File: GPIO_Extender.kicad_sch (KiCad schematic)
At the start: 22 parts, among them IC1 PCA9575PW2,118

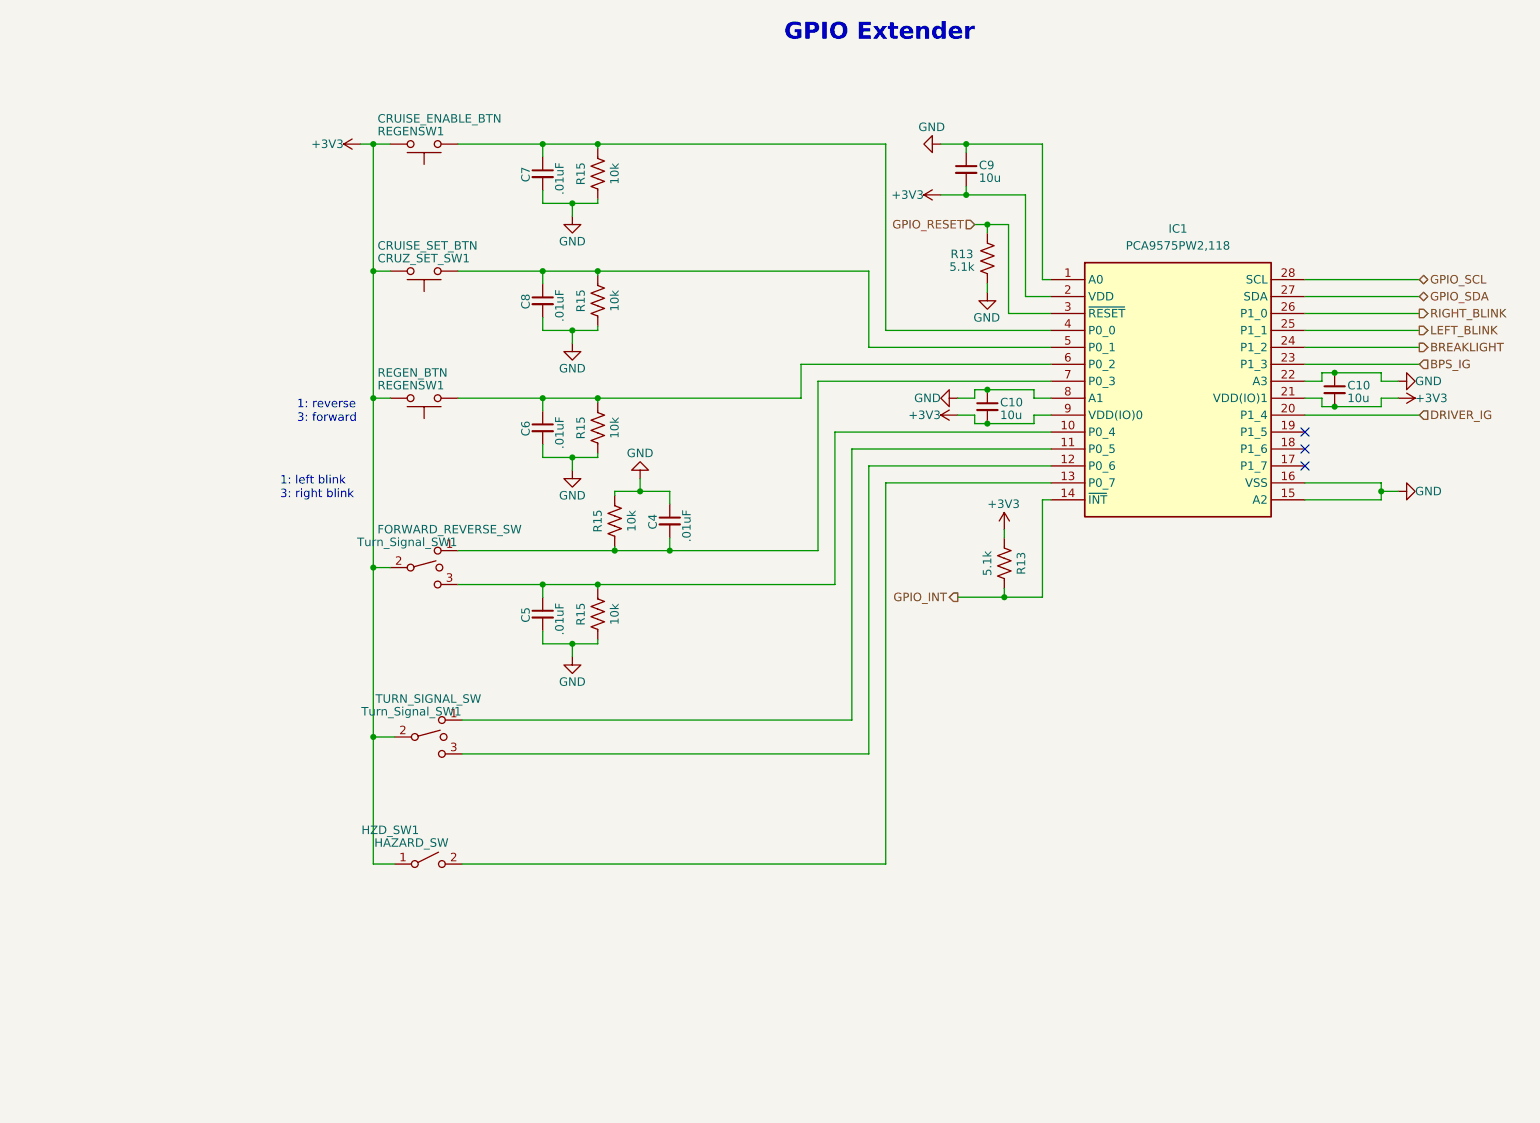
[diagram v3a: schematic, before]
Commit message: added notes section to bottom of sheets
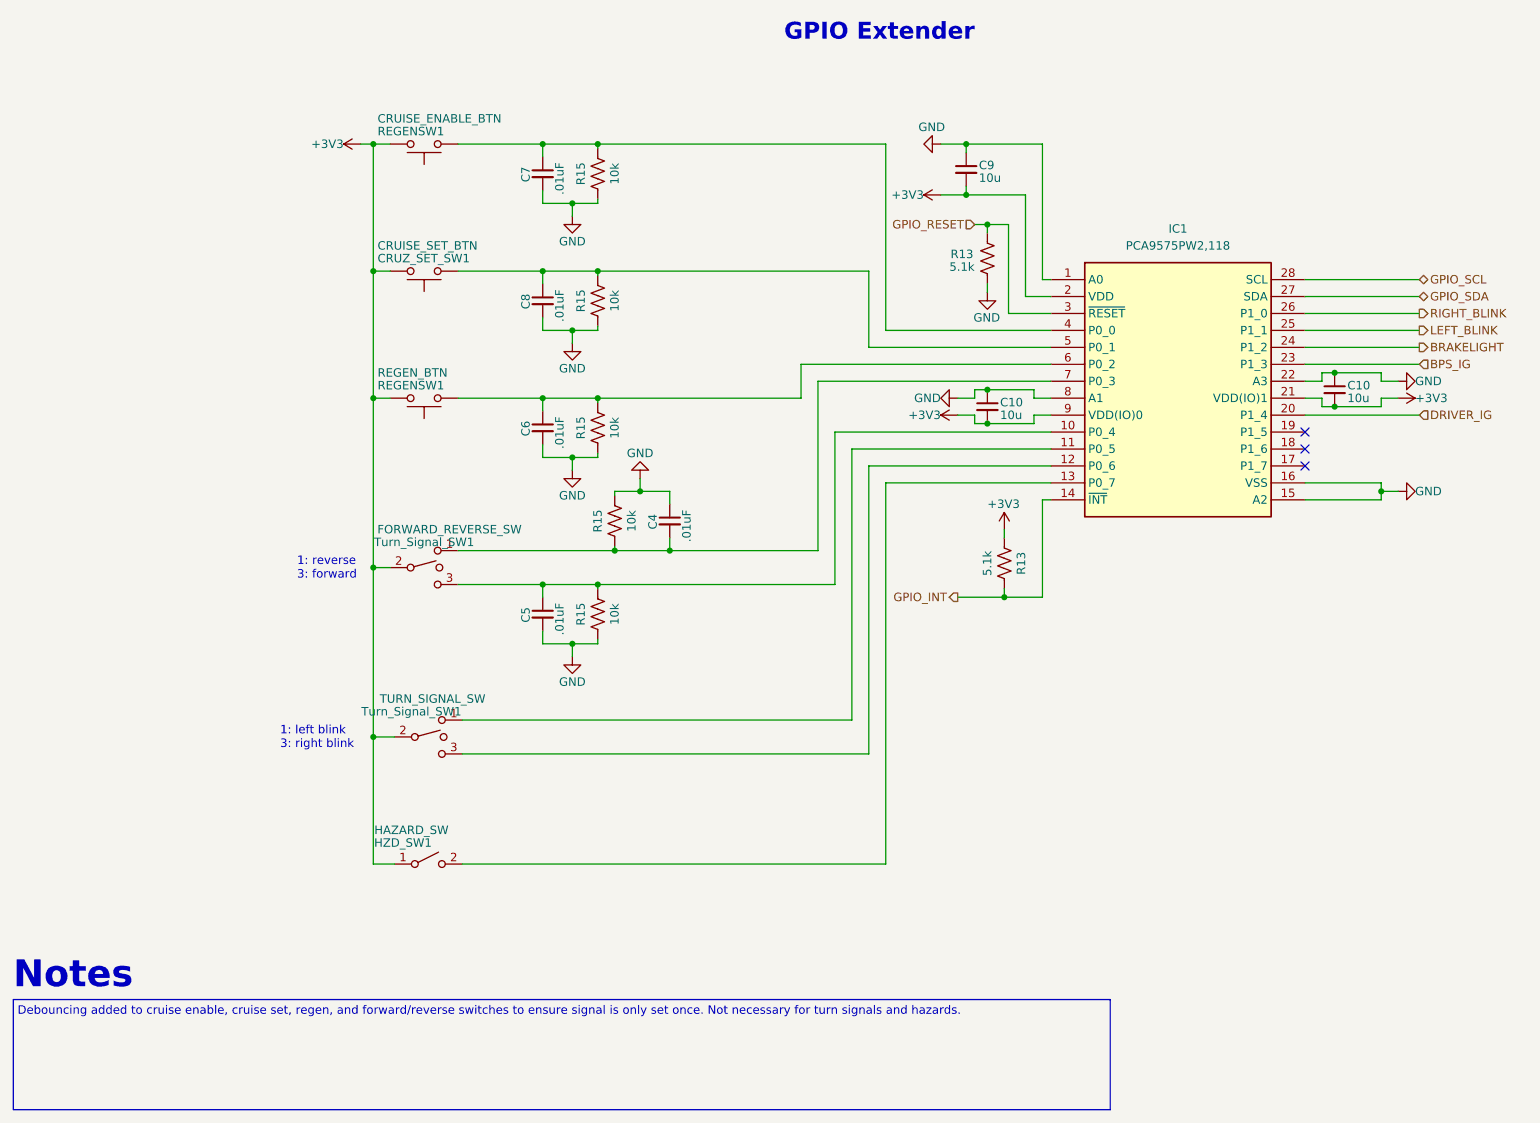
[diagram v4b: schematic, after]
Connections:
- net BREAKLIGHT renamed BRAKELIGHT
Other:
- note added: "Debouncing added to cruise enable, cruise set, regen, and forward/reverse switches to ensure signal is only set once. Not necessary for turn signals and hazards."
- note added: "Notes"
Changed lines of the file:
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@@
     (stroke (width 0) (type default))
   )
-  (text "1: left blink\n3: right blink" (at 52.07 106.68 0)
+  (rectangle (start 12.065 181.61) (end 176.53 198.12)
+    (stroke (width 0) (type default))
+    (fill (type none))
+  )
+  (text "1: left blink\n3: right blink" (at 52.07 144.145 0)
     (effects (font (size 1.27 1.27)) (justify left bottom))
   )
-  (text "1: reverse\n3: forward" (at 54.61 95.25 0)
+  (text "1: reverse\n3: forward" (at 54.61 118.745 0)
     (effects (font (size 1.27 1.27)) (justify left bottom))
+  )
+  (text "Notes" (at 12.065 180.34 0)
+    (effects (font (size 4 4) (thickness 0.8) bold) (justify left bottom))
   )
   (text "GPIO Extender" (at 127.635 38.1 0)
     (effects (font (size 2.54 2.54) (thickness 0.508) bold) (justify left bottom))
   )
+  (text "Debouncing added to cruise enable, cruise set, regen, and forward/reverse switches to ensure signal is only set once. Not necessary for turn signals and hazards."
+    (at 12.7 184.15 0)
+    (effects (font (size 1.27 1.27)) (justify left bottom))
+  )
   (hierarchical_label "DRIVER_IG" (shape input) (at 222.885 93.98 0) (fields_autoplaced)
     (effects (font (size 1.27 1.27)) (justify left))
@@
     (effects (font (size 1.27 1.27)) (justify left))
   )
-  (hierarchical_label "BREAKLIGHT" (shape output) (at 222.885 83.82 0) (fields_autoplaced)
+  (hierarchical_label "BRAKELIGHT" (shape output) (at 222.885 83.82 0) (fields_autoplaced)
     (effects (font (size 1.27 1.27)) (justify left))
   )
@@
         )
         (path "/c7871779-04fe-4705-8150-20a4dd0ef44f/2112f985-b932-45cd-8ebe-65af3370f212"
-          (reference "REGENSW2") (unit 1)
+          (reference "REGEN_SW1") (unit 1)
         )
       )
@@
   (symbol (lib_id "Switch:SW_SPDT_MSM") (at 73.66 116.84 0) (unit 1)
     (in_bom yes) (on_board yes) (dnp no)
-    (property "Reference" "Turn_Signal_SW1" (at 71.12 113.03 0)
+    (property "Reference" "Turn_Signal_SW1" (at 73.66 113.03 0)
       (effects (font (size 1.27 1.27)))
     )
@@
         )
         (path "/c7871779-04fe-4705-8150-20a4dd0ef44f/2112f985-b932-45cd-8ebe-65af3370f212"
-          (reference "Turn_Signal_SW1") (unit 1)
+          (reference "FOR_REV_SW1") (unit 1)
         )
       )
@@
       (effects (font (size 1.27 1.27)))
     )
-    (property "Value" "TURN_SIGNAL_SW" (at 74.295 136.525 0)
+    (property "Value" "TURN_SIGNAL_SW" (at 74.93 136.525 0)
       (effects (font (size 1.27 1.27)))
     )
@@
         )
         (path "/c7871779-04fe-4705-8150-20a4dd0ef44f/2112f985-b932-45cd-8ebe-65af3370f212"
-          (reference "Turn_Signal_SW2") (unit 1)
+          (reference "TURN_SW1") (unit 1)
         )
       )
@@
         )
         (path "/c7871779-04fe-4705-8150-20a4dd0ef44f/2112f985-b932-45cd-8ebe-65af3370f212"
-          (reference "REGENSW1") (unit 1)
+          (reference "CRUZ_EN_SW1") (unit 1)
         )
       )
@@
   (symbol (lib_id "Switch:SW_SPST") (at 74.295 161.29 0) (unit 1)
     (in_bom yes) (on_board yes) (dnp no)
-    (property "Reference" "HZD_SW1" (at 68.58 156.21 0)
-      (effects (font (size 1.27 1.27)))
-    )
-    (property "Value" "HAZARD_SW" (at 71.755 158.115 0)
-      (effects (font (size 1.27 1.27)))
-    )
+    (property "Reference" "HZD_SW1" (at 70.485 158.115 0)
+      (effects (font (size 1.27 1.27)))
+    )
+    (property "Value" "HAZARD_SW" (at 71.755 156.21 0)
+      (effects (font (size 1.27 1.27)))
+    )

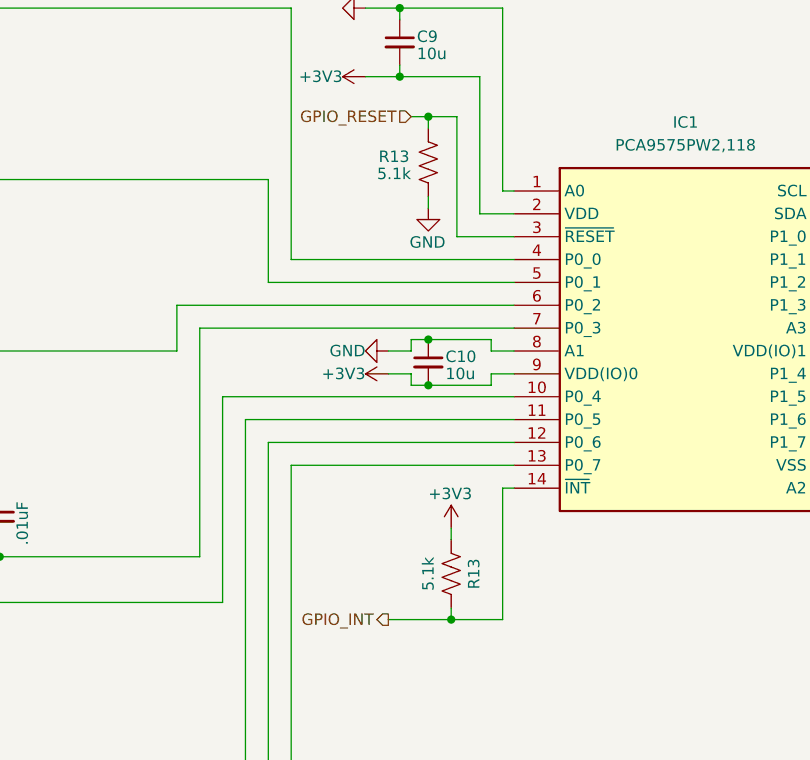
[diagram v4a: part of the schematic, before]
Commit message: Added to notes and changed resistor values
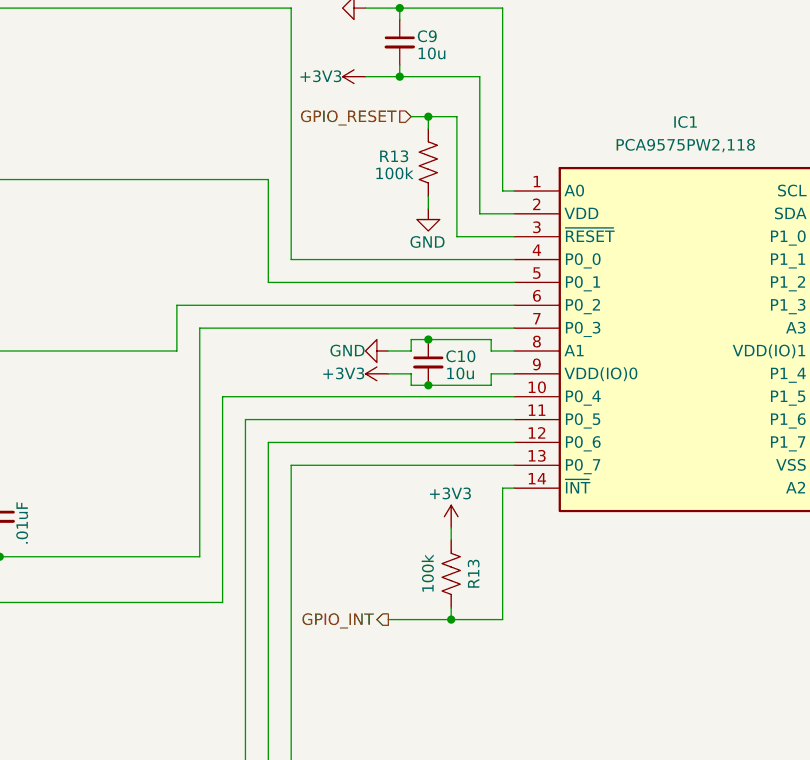
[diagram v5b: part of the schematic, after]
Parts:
- R13: value 5.1k -> 100k
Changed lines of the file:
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@@
       (effects (font (size 1.27 1.27)))
     )
-    (property "Value" "5.1k" (at 154.305 71.755 0)
+    (property "Value" "100k" (at 154.305 71.755 0)
       (effects (font (size 1.27 1.27)))
     )
@@
       (effects (font (size 1.27 1.27)))
     )
-    (property "Value" "5.1k" (at 158.115 116.205 90)
+    (property "Value" "100k" (at 158.115 116.205 90)
       (effects (font (size 1.27 1.27)))
     )
